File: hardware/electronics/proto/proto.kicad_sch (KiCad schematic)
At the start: 49 parts, among them J1 Conn_01x08_Female, U1 ADS131M06, U2 AP131-30

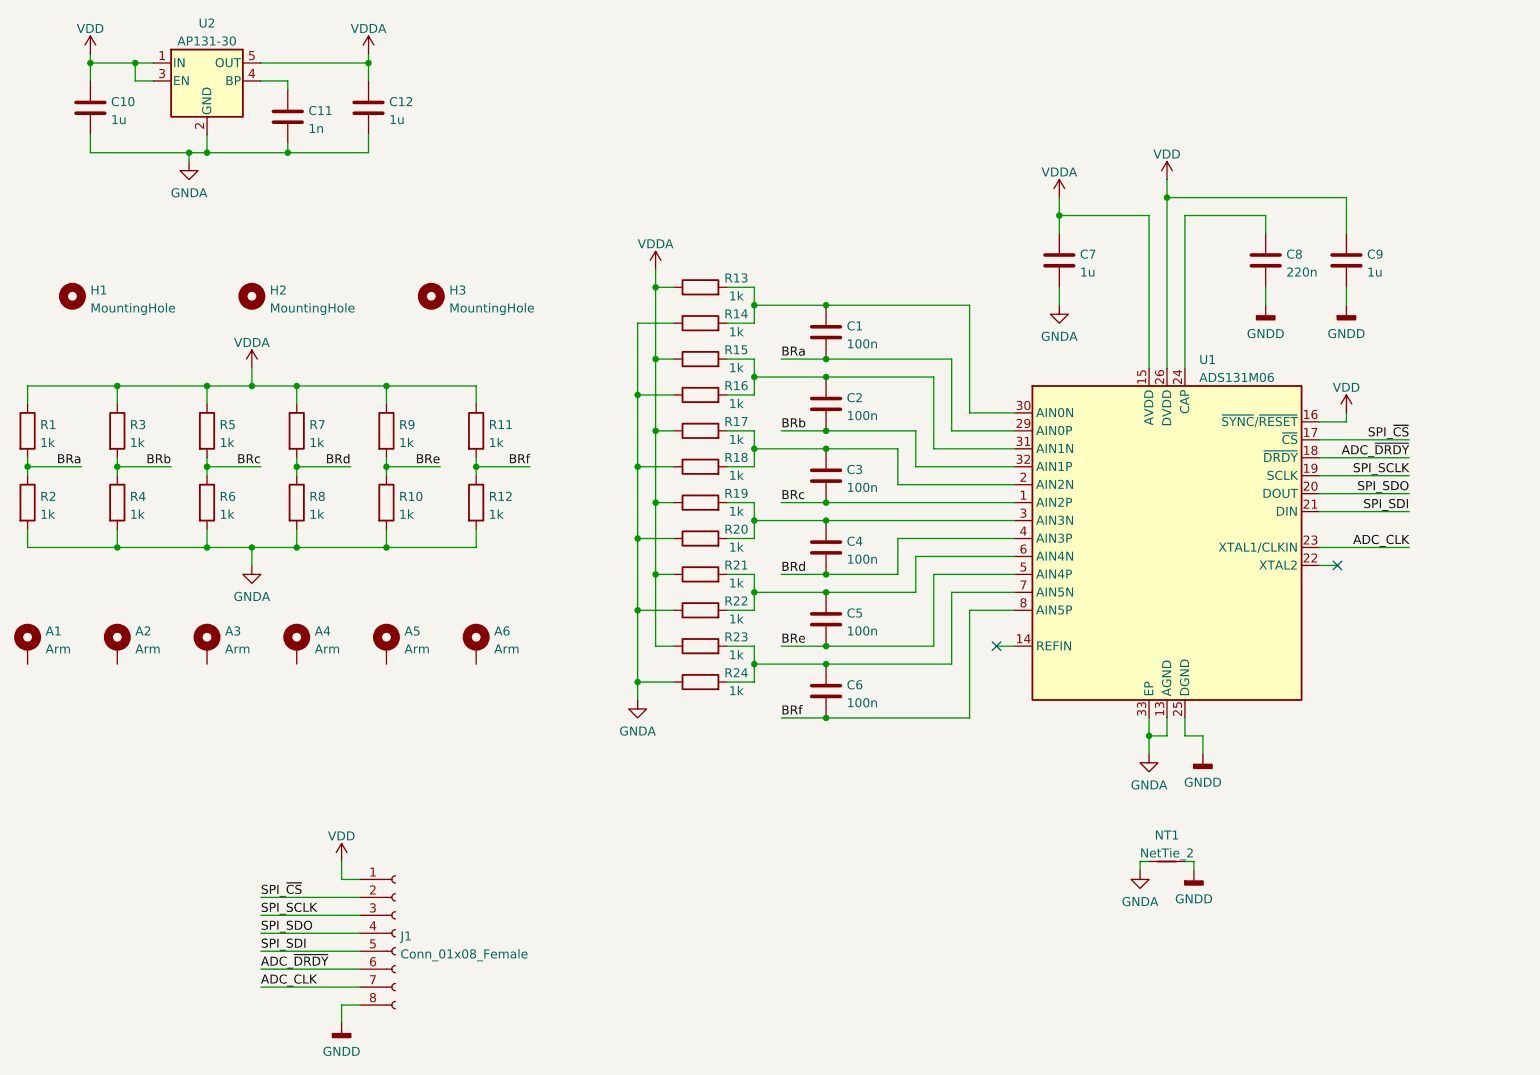
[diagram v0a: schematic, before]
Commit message: Use strain gauges instead of thick film resistors (#8)
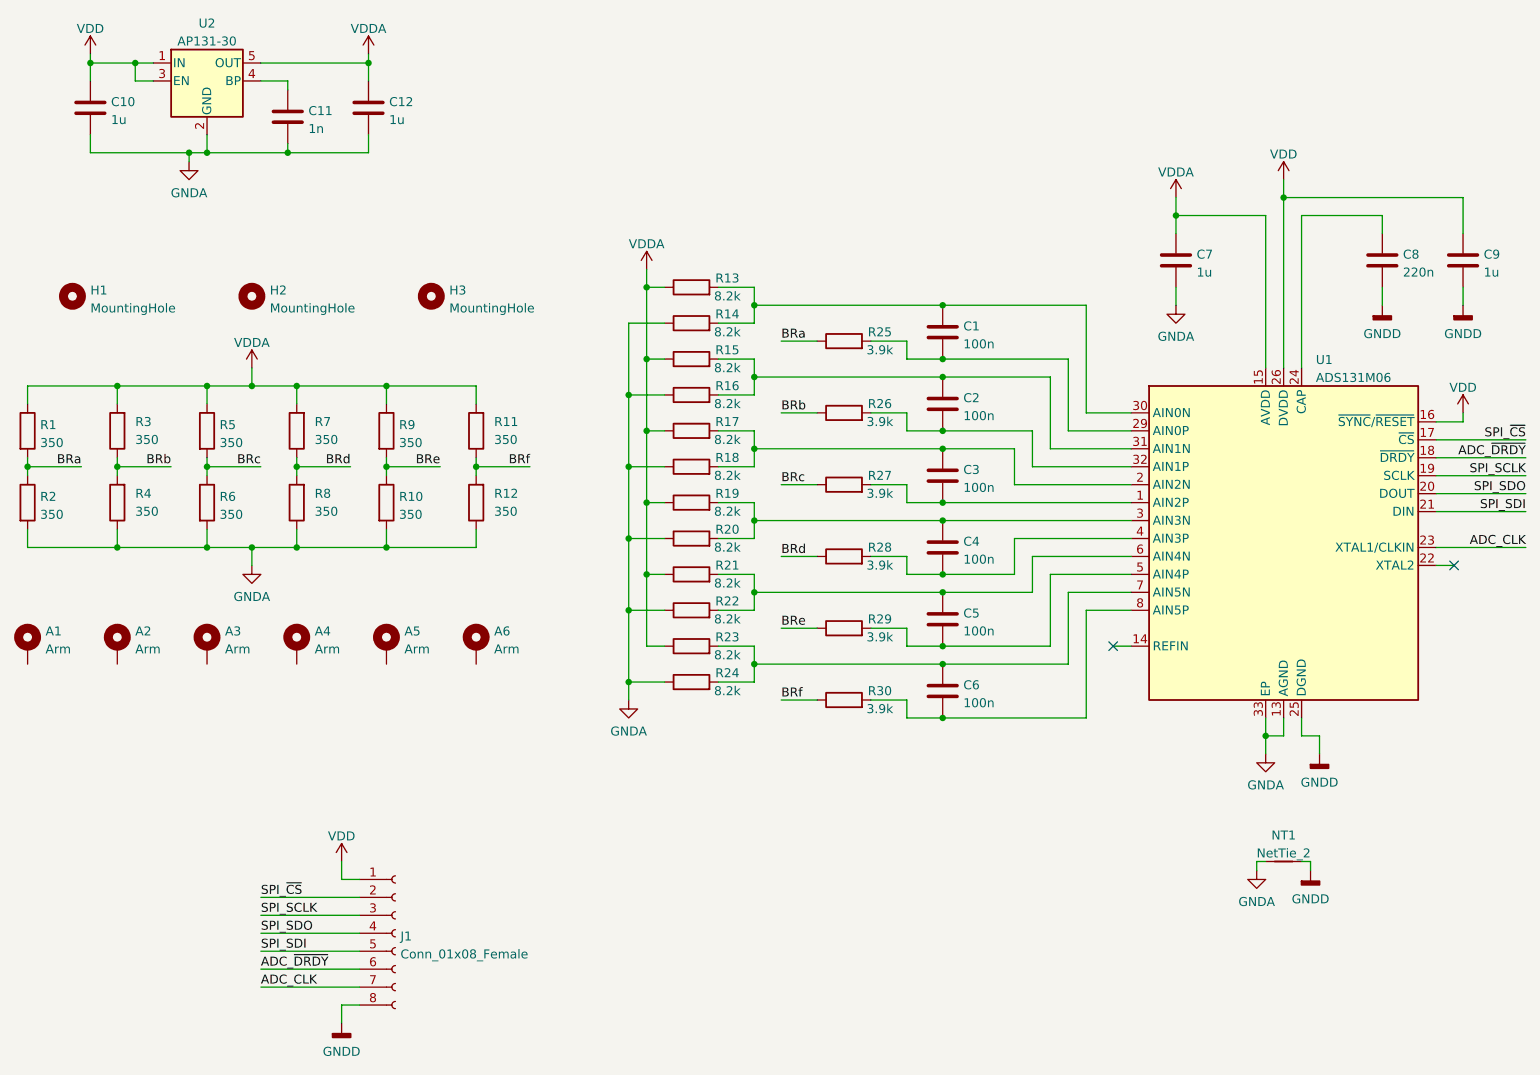
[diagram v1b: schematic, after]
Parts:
- added R25, R26, R27, R28, R29, R30: 3.9k, Resistor_SMD:R_0603_1608Metric_Pad0.98x0.95mm_HandSolder, symbol Device:R
- R1, R10, R11, R12, R2, R3, R4, R5, R6, R7, R8, R9: value 1k -> 350; footprint Resistor_SMD:R_2512_6332Metric_Pad1.40x3.35mm_HandSolder -> proto:StrainGauge_BF350-3AA
- R13, R14, R15, R16, R17, R18, R19, R20, R21, R22, R23, R24: value 1k -> 8.2k
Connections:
- net BRa: now also R25.1; no longer C1.2, U1.29 (AIN0P)
- net BRb: now also R3.1, R4.2, R26.1; no longer C2.2, R3.2, R4.1, U1.32 (AIN1P)
- net BRc: now also R27.1; no longer C3.2, U1.1 (AIN2P)
- net BRd: now also R7.1, R8.2, R28.1; no longer C4.2, R7.2, R8.1, U1.4 (AIN3P)
- net BRe: now also R29.1; no longer C5.2, U1.5 (AIN4P)
- net BRf: now also R11.1, R12.2, R30.1; no longer C6.2, R11.2, R12.1, U1.8 (AIN5P)
- net GNDA: now also R12.1, R4.1, R8.1; no longer R12.2, R4.2, R8.2
- net VDDA: now also R11.2, R3.2, R7.2; no longer R11.1, R3.1, R7.1
- new net: C1.2, R25.2, U1.29 (AIN0P)
- new net: C6.2, R30.2, U1.8 (AIN5P)
- new net: C4.2, R28.2, U1.4 (AIN3P)
- new net: C2.2, R26.2, U1.32 (AIN1P)
- new net: C3.2, R27.2, U1.1 (AIN2P)
- new net: C5.2, R29.2, U1.5 (AIN4P)
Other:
- moved on the sheet: C1, C2, C3, C4, C5, C6, C7, C8, C9, NT1, R11, R12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
